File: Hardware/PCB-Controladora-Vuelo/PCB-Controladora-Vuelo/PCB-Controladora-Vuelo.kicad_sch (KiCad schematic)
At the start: 16 parts, among them J1 Jumper Serial, J2 ESC, U1 MPU-5060, U2 ESP32-DEVKIT-V1, U2 Nrf24l01, U3 AMS1117-3.3

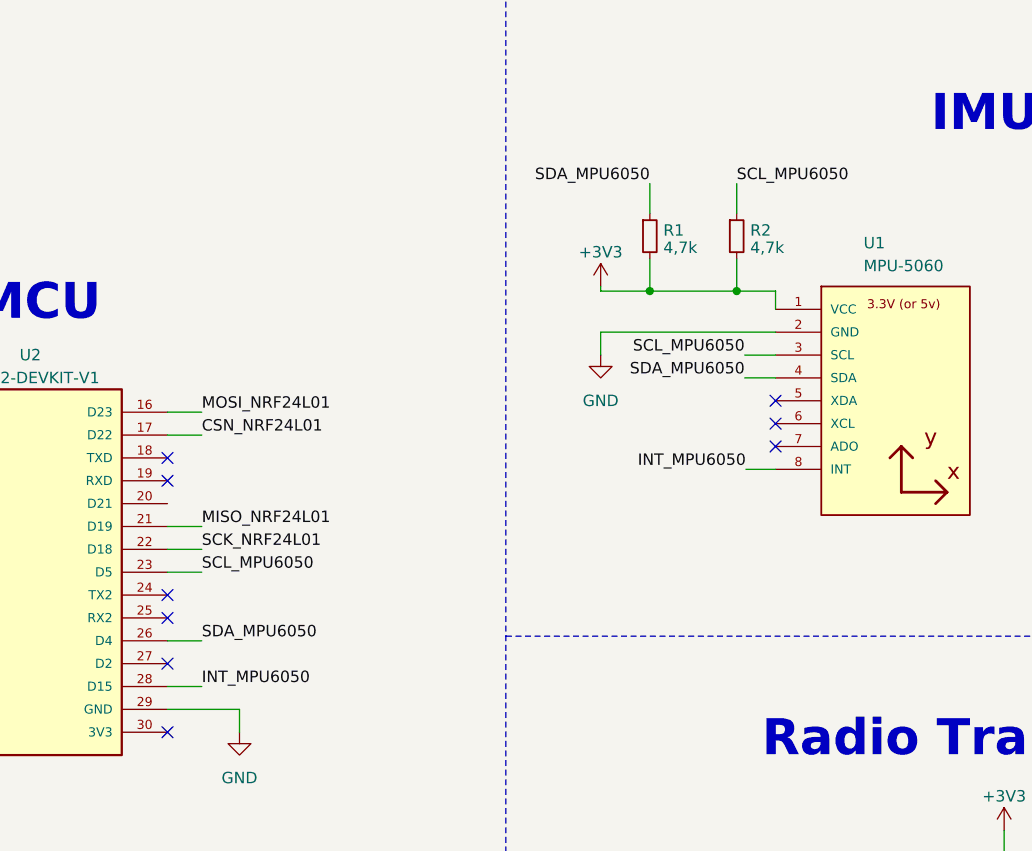
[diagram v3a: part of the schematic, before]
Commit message: placa realizada en taller , prueba de pines
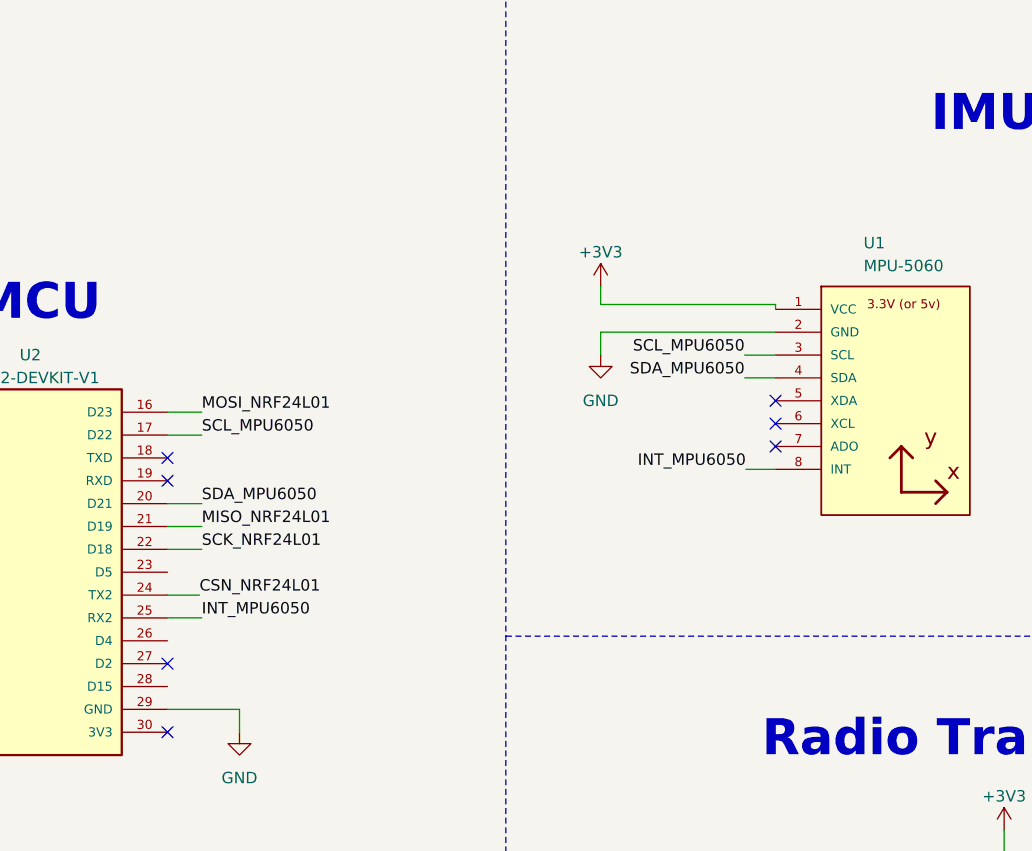
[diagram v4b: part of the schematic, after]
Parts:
- removed R1, R2: 4,7k, Resistor_SMD:R_1206_3216Metric_Pad1.30x1.75mm_HandSolder, symbol Device:R_Small
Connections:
- net CSN_NRF24L01: now also U2.24 (TX2); no longer U2.17 (D22)
- net INT_MPU6050: now also U2.25 (RX2); no longer U2.28 (D15)
- net SCL_MPU6050: now also U2.17 (D22); no longer U2.23 (D5)
- net SDA_MPU6050: now also U2.20 (D21); no longer U2.26 (D4)
- no-connect marks 22 -> 20
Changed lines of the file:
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@@
   (junction (at 49.784 61.722) (diameter 0) (color 0 0 0 0)
   )
-  (junction (at 202.946 46.228) (diameter 0) (color 0 0 0 0)
-  )
   (junction (at 28.448 51.562) (diameter 0) (color 0 0 0 0)
   )
@@
   (junction (at 28.448 61.722) (diameter 0) (color 0 0 0 0)
   )
-  (junction (at 193.294 46.228) (diameter 0) (color 0 0 0 0)
-  )
   (junction (at 49.784 51.562) (diameter 0) (color 0 0 0 0)
   )
@@
   (no_connect (at 109.22 64.77))
   (no_connect (at 207.264 60.96))
-  (no_connect (at 139.7 82.55))
   (no_connect (at 109.22 85.09))
   (no_connect (at 139.7 67.31))
@@
   (no_connect (at 41.275 107.95))
   (no_connect (at 41.275 130.81))
-  (no_connect (at 139.7 80.01))
   (wire (pts (xy 147.701 95.25) (xy 147.701 92.71))
     (stroke (width 0) (type default))
@@
     (stroke (width 0) (type default))
   )
-  (wire (pts (xy 187.833 45.72) (xy 187.833 46.228))
-    (stroke (width 0) (type default))
-  )
   (wire (pts (xy 22.098 60.452) (xy 22.098 61.722))
     (stroke (width 0) (type default))
@@
     (stroke (width 0) (type default))
   )
+  (wire (pts (xy 187.833 47.7266) (xy 187.833 45.72))
+    (stroke (width 0) (type default))
+  )
   (wire (pts (xy 105.664 77.47) (xy 109.22 77.47))
     (stroke (width 0) (type default))
@@
     (stroke (width 0) (type default))
   )
-  (wire (pts (xy 202.946 46.228) (xy 207.264 46.228))
-    (stroke (width 0) (type default))
-  )
   (wire (pts (xy 203.835 55.88) (xy 207.264 55.88))
     (stroke (width 0) (type default))
@@
     (stroke (width 0) (type default))
   )
-  (wire (pts (xy 139.7 77.47) (xy 143.51 77.47))
-    (stroke (width 0) (type default))
-  )
   (wire (pts (xy 105.664 82.55) (xy 109.22 82.55))
     (stroke (width 0) (type default))
@@
     (stroke (width 0) (type default))
   )
-  (wire (pts (xy 193.294 46.228) (xy 202.946 46.228))
+  (wire (pts (xy 187.833 47.7266) (xy 207.264 47.7266))
     (stroke (width 0) (type default))
   )
-  (wire (pts (xy 47.498 51.562) (xy 49.784 51.562))
+  (wire (pts (xy 139.7 69.85) (xy 143.51 69.85))
     (stroke (width 0) (type default))
   )
-  (wire (pts (xy 193.294 34.29) (xy 193.294 37.592))
+  (wire (pts (xy 47.498 51.562) (xy 49.784 51.562))
     (stroke (width 0) (type default))
   )
@@
     (stroke (width 0) (type default))
   )
-  (wire (pts (xy 187.833 46.228) (xy 193.294 46.228))
-    (stroke (width 0) (type default))
-  )
   (wire (pts (xy 106.172 95.25) (xy 109.22 95.25))
     (stroke (width 0) (type default))
@@
     (stroke (width 0) (type default))
   )
+  (wire (pts (xy 139.7 80.01) (xy 143.256 80.01))
+    (stroke (width 0) (type default))
+  )
   (wire (pts (xy 22.098 61.722) (xy 28.448 61.722))
     (stroke (width 0) (type default))
@@
     (stroke (width 0) (type default))
   )
-  (wire (pts (xy 49.784 51.562) (xy 49.784 52.832))
+  (wire (pts (xy 143.51 82.55) (xy 139.7 82.55))
     (stroke (width 0) (type default))
   )
-  (wire (pts (xy 193.294 42.672) (xy 193.294 46.228))
+  (wire (pts (xy 49.784 51.562) (xy 49.784 52.832))
     (stroke (width 0) (type default))
   )
@@
     (stroke (width 0) (type default))
   )
+  (wire (pts (xy 207.264 47.7266) (xy 207.264 48.26))
+    (stroke (width 0) (type default))
+  )
   (wire (pts (xy 105.664 72.39) (xy 109.22 72.39))
     (stroke (width 0) (type default))
@@
     (stroke (width 0) (type default))
   )
-  (wire (pts (xy 202.946 34.29) (xy 202.946 37.592))
-    (stroke (width 0) (type default))
-  )
   (wire (pts (xy 139.7 59.69) (xy 143.51 59.69))
     (stroke (width 0) (type default))
@@
     (stroke (width 0) (type dash))
   )
-  (wire (pts (xy 143.51 90.17) (xy 139.7 90.17))
-    (stroke (width 0) (type default))
-  )
-  (wire (pts (xy 202.946 42.672) (xy 202.946 46.228))
-    (stroke (width 0) (type default))
-  )
   (wire (pts (xy 143.51 62.23) (xy 139.7 62.23))
     (stroke (width 0) (type default))
@@
     (stroke (width 0) (type default))
   )
-  (wire (pts (xy 207.264 46.228) (xy 207.264 48.26))
-    (stroke (width 0) (type default))
-  )
   (polyline (pts (xy 11.9888 144.78) (xy 71.12 144.78))
     (stroke (width 0) (type default))
@@
     (stroke (width 0) (type default))
   )
-  (wire (pts (xy 139.7 85.09) (xy 143.51 85.09))
-    (stroke (width 0) (type default))
-  )
   (wire (pts (xy 39.878 65.532) (xy 39.878 61.722))
     (stroke (width 0) (type default))
@@
     (effects (font (size 1.27 1.27)) (justify right bottom))
   )
+  (label "CSN_NRF24L01" (at 143.256 80.01 0) (fields_autoplaced)
+    (effects (font (size 1.27 1.27)) (justify left bottom))
+  )
   (label "SCL_MPU6050" (at 203.835 53.34 180) (fields_autoplaced)
     (effects (font (size 1.27 1.27)) (justify right bottom))
   )
-  (label "SCL_MPU6050" (at 202.946 34.29 0) (fields_autoplaced)
-    (effects (font (size 1.27 1.27)) (justify left bottom))
-  )
   (label "S3_MOTOR" (at 105.664 77.47 180) (fields_autoplaced)
     (effects (font (size 1.27 1.27)) (justify right bottom))
@@
     (effects (font (size 1.27 1.27)) (justify right bottom))
   )
+  (label "SCL_MPU6050" (at 143.51 62.23 0) (fields_autoplaced)
+    (effects (font (size 1.27 1.27)) (justify left bottom))
+  )
   (label "S2_MOTOR" (at 37.465 120.65 180) (fields_autoplaced)
     (effects (font (size 1.27 1.27)) (justify right bottom))
@@
     (effects (font (size 1.27 1.27)) (justify right bottom))
   )
-  (label "SDA_MPU6050" (at 193.294 34.29 180) (fields_autoplaced)
-    (effects (font (size 1.27 1.27)) (justify right bottom))
-  )
   (label "S2_MOTOR" (at 105.664 74.93 180) (fields_autoplaced)
     (effects (font (size 1.27 1.27)) (justify right bottom))
@@
     (effects (font (size 1.27 1.27) bold) (justify left bottom))
   )
-  (label "INT_MPU6050" (at 143.51 90.17 0) (fields_autoplaced)
-    (effects (font (size 1.27 1.27)) (justify left bottom))
-  )
   (label "INT_MPU6050" (at 203.962 66.04 180) (fields_autoplaced)
     (effects (font (size 1.27 1.27)) (justify right bottom))
   )
-  (label "SCL_MPU6050" (at 143.51 77.47 0) (fields_autoplaced)
+  (label "SDA_MPU6050" (at 143.51 69.85 0) (fields_autoplaced)
+    (effects (font (size 1.27 1.27)) (justify left bottom))
+  )
+  (label "INT_MPU6050" (at 143.51 82.55 0) (fields_autoplaced)
     (effects (font (size 1.27 1.27)) (justify left bottom))
   )
@@
     (effects (font (size 1.27 1.27)) (justify right bottom))
   )
-  (label "CSN_NRF24L01" (at 143.51 62.23 0) (fields_autoplaced)
-    (effects (font (size 1.27 1.27)) (justify left bottom))
-  )
   (label "S1_MOTOR" (at 37.465 118.11 180) (fields_autoplaced)
     (effects (font (size 1.27 1.27)) (justify right bottom))
   )
-  (label "SDA_MPU6050" (at 143.51 85.09 0) (fields_autoplaced)
-    (effects (font (size 1.27 1.27)) (justify left bottom))
-  )
   (symbol (lib_id "power:GND") (at 31.115 102.87 180) (unit 1)
     (in_bom yes) (on_board yes) (dnp no) (fields_autoplaced)
@@
     (pin "25")
     (pin "26")
-    (pin "28")
     (pin "27")
+    (pin "28")
     (pin "3")
     (pin "30")
@@
     )
   )
-  (symbol (lib_id "Device:R_Small") (at 202.946 40.132 0) (unit 1)
-    (in_bom yes) (on_board yes) (dnp no) (fields_autoplaced)
-    (property "Reference" "R2" (at 204.4446 39.4883 0)
-      (effects (font (size 1.27 1.27)) (justify left))
-    )
-    (property "Value" "4,7k" (at 204.4446 41.4093 0)
-      (effects (font (size 1.27 1.27)) (justify left))
-    )
-    (property "Footprint" "Resistor_SMD:R_1206_3216Metric_Pad1.30x1.75mm_HandSolder" (at 202.946 40.132 0)
-      (effects (font (size 1.27 1.27)) hide)
-    )
-    (property "Datasheet" "~" (at 202.946 40.132 0)
-      (effects (font (size 1.27 1.27)) hide)
-    )
-    (pin "1")
-    (pin "2")
-    (instances
-      (project "PCB-Controladora-Vuelo"
-        (path "/ac5864b2-231c-45bd-8efa-594ea27cde2d"
-          (reference "R2") (unit 1)
-        )
-      )
-    )
-  )
   (symbol (lib_id "power:GND") (at 86.868 95.25 0) (unit 1)
     (in_bom yes) (on_board yes) (dnp no) (fields_autoplaced)
@@
         )
       )
-    )
-  )
-  (symbol (lib_id "Device:R_Small") (at 193.294 40.132 0) (unit 1)
-    (in_bom yes) (on_board yes) (dnp no) (fields_autoplaced)
-    (property "Reference" "R1" (at 194.7926 39.4883 0)
-      (effects (font (size 1.27 1.27)) (justify left))
-    )
-    (property "Value" "4,7k" (at 194.7926 41.4093 0)
-      (effects (font (size 1.27 1.27)) (justify left))
-    )
-    (property "Footprint" "Resistor_SMD:R_1206_3216Metric_Pad1.30x1.75mm_HandSolder" (at 193.294 40.132 0)
-      (effects (font (size 1.27 1.27)) hide)
-    )
-    (property "Datasheet" "~" (at 193.294 40.132 0)
-      (effects (font (size 1.27 1.27)) hide)
-    )
-    (pin "1")
-    (pin "2")
-    (instances
-      (project "PCB-Controladora-Vuelo"
-        (path "/ac5864b2-231c-45bd-8efa-594ea27cde2d"
-          (reference "R1") (unit 1)
-        )
-      )
